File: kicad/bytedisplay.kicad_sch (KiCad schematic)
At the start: 6 parts, among them J1 LObits, J2 HIbits, J3 PGM, U1 ATtiny1616-S, U2 HSN-3621

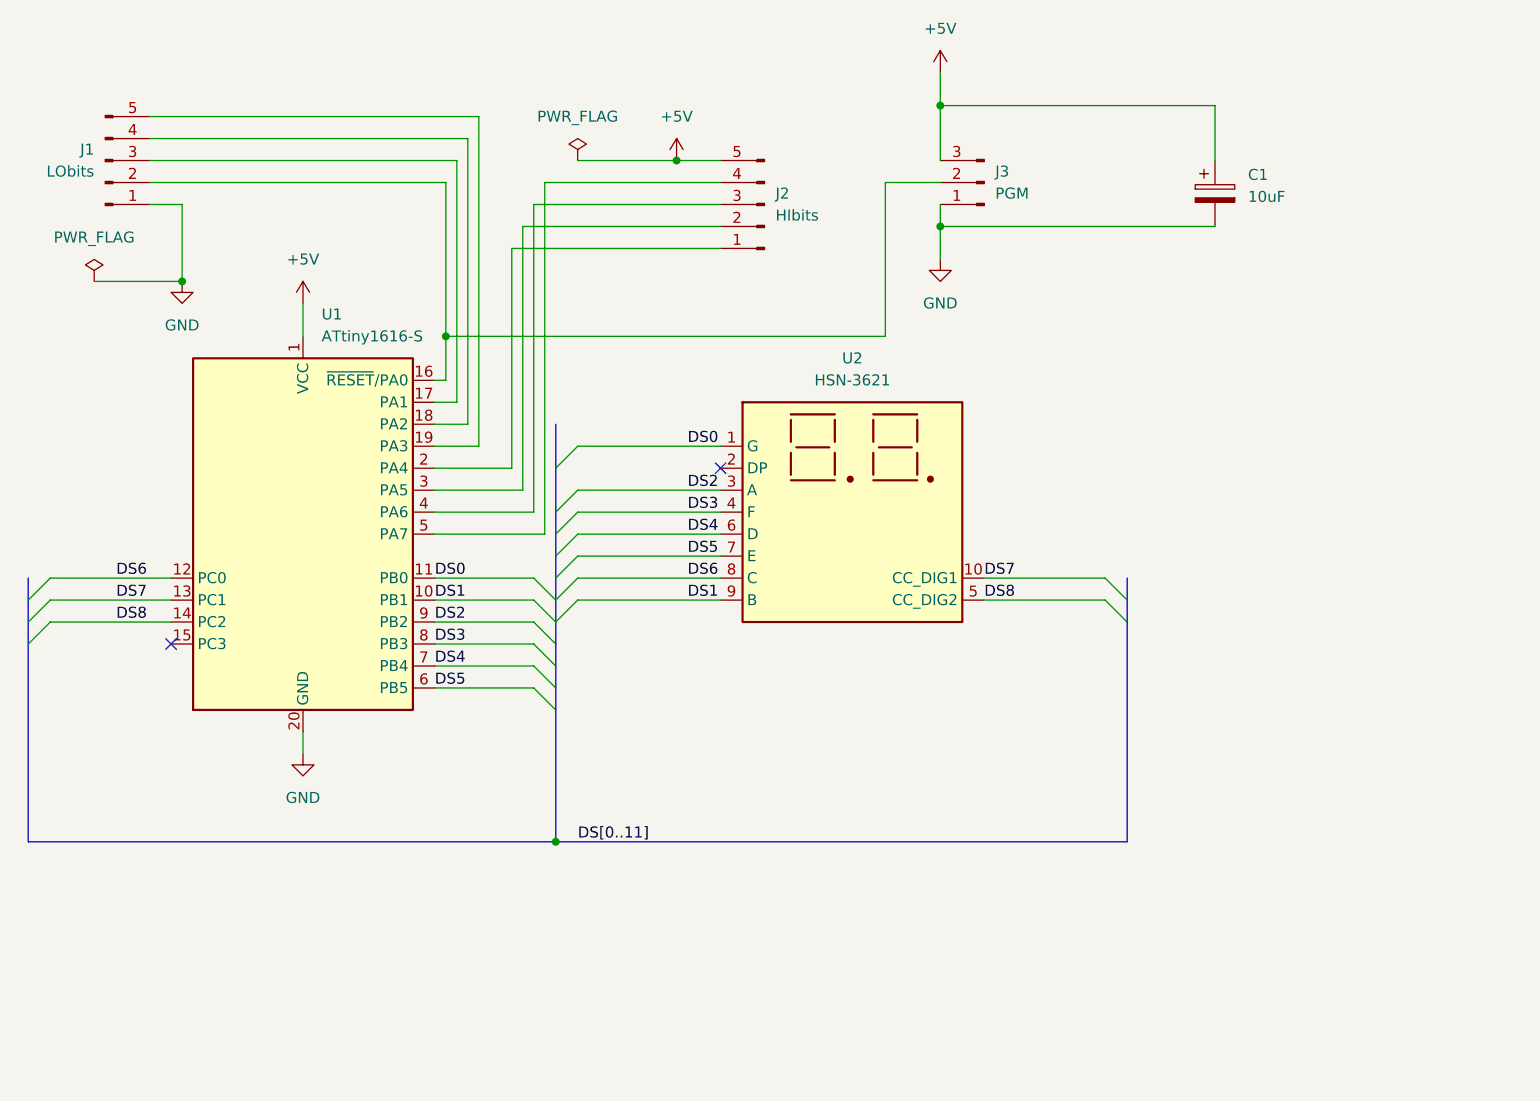
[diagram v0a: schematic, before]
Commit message: [kicad] Move symbols to project library
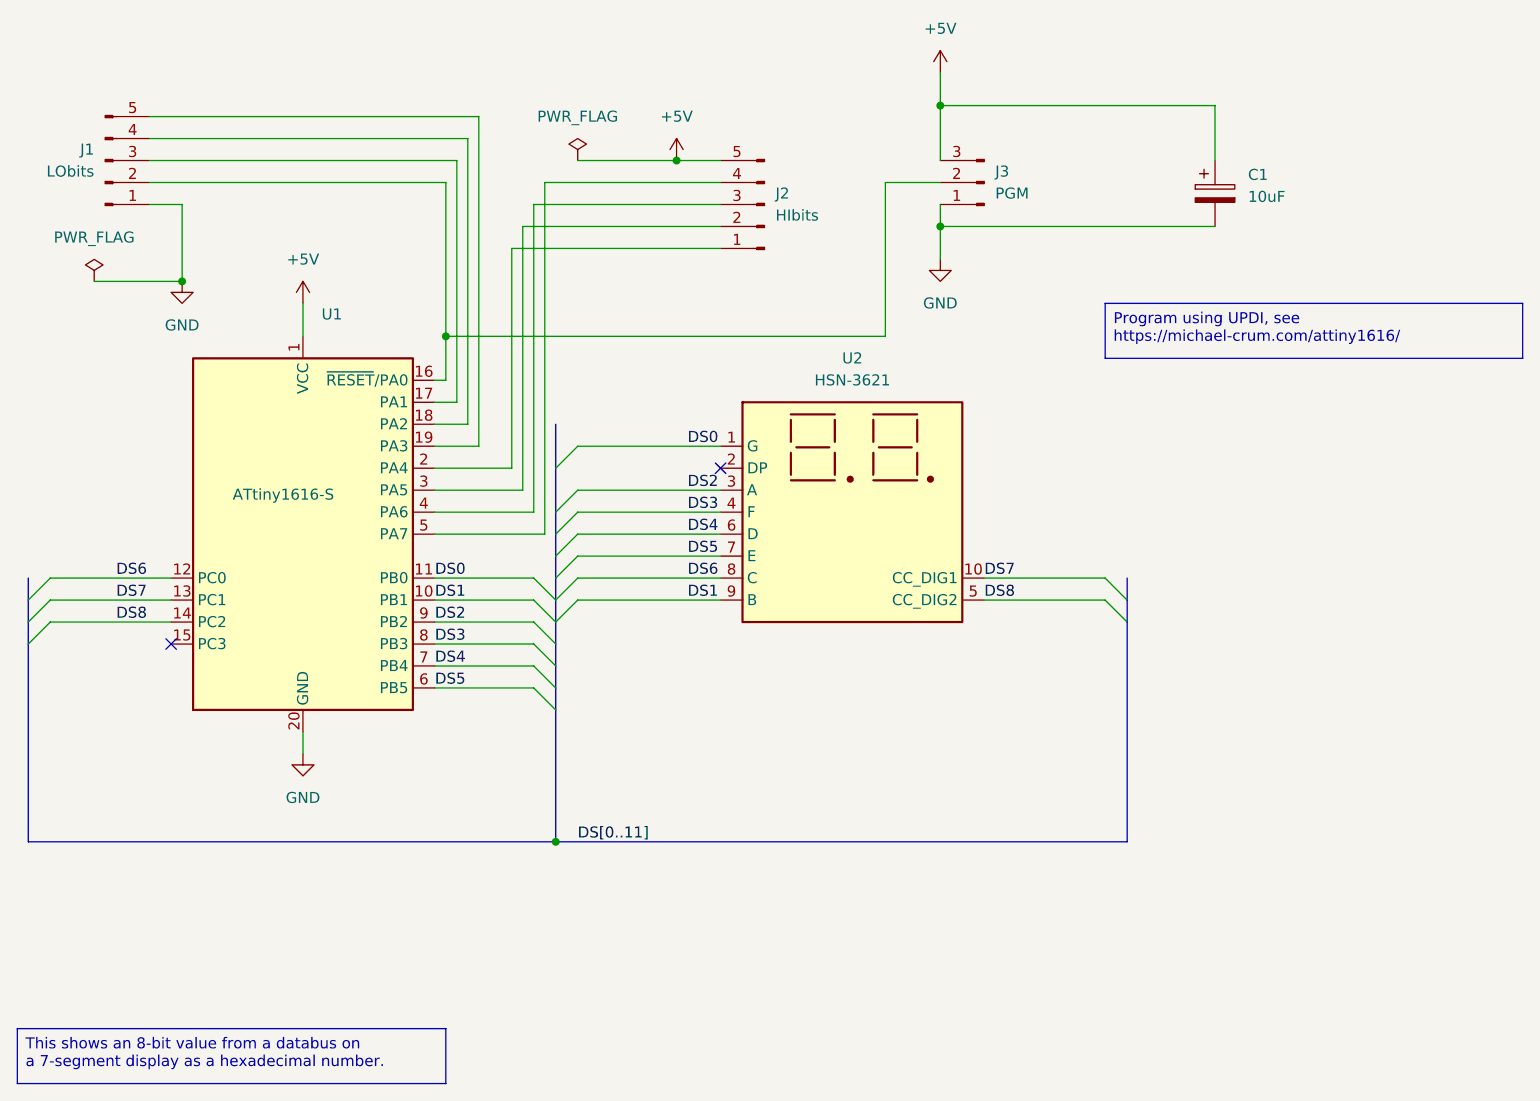
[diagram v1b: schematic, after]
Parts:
- C1: symbol Device:C_Polarized -> Library:C_Polarized
- J1, J2: symbol Connector:Conn_01x05_Pin -> Library:Conn_01x05_Pin
- J3: symbol Connector:Conn_01x03_Pin -> Library:Conn_01x03_Pin
- U1: symbol MCU_Microchip_ATtiny:ATtiny1616-S -> Library:ATtiny1616-S
- U2: symbol Display_Character:HDSM-443B -> Library:HDSM-443B
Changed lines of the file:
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@@
 		(company "ErrorSoft")
+	)
+	(text_box "This shows an 8-bit value from a databus on\na 7-segment display as a hexadecimal number."
+		(exclude_from_sim no)
+		(at 45.72 149.86 0)
+		(size 49.53 6.35)
+		(margins 0.9525 0.9525 0.9525 0.9525)
+		(stroke
+			(width 0)
+			(type solid)
+		)
+		(fill
+			(type none)
+		)
+		(effects
+			(font
+				(size 1.27 1.27)
+			)
+			(justify left top)
+		)
+	)
+	(text_box "Program using UPDI, see\nhttps://michael-crum.com/attiny1616/"
+		(exclude_from_sim no)
+		(at 171.45 66.04 0)
+		(size 48.26 6.35)
+		(margins 0.9525 0.9525 0.9525 0.9525)
+		(stroke
+			(width 0)
+			(type solid)
+		)
+		(fill
+			(type color)
+			(color 0 255 0 1)
+		)
+		(effects
+			(font
+				(size 1.27 1.27)
+			)
+			(justify left top)
+		)
 	)
 	(junction
@@
 	)
 	(symbol
-		(lib_id "Device:C_Polarized")
+		(lib_id "Library:C_Polarized")
 		(at 184.15 53.34 0)
 		(unit 1)
@@
 	)
 	(symbol
-		(lib_id "Display_Character:HDSM-443B")
+		(lib_id "Library:HDSM-443B")
 		(at 142.24 90.17 0)
 		(unit 1)
@@
 	)
 	(symbol
-		(lib_id "MCU_Microchip_ATtiny:ATtiny1616-S")
+		(lib_id "Library:ATtiny1616-S")
 		(at 78.74 92.71 0)
 		(unit 1)
@@
 		(on_board yes)
 		(dnp no)
-		(fields_autoplaced yes)
 		(property "Reference" "U1"
 			(at 80.8833 67.31 0)
@@
 		)
 		(property "Value" "ATtiny1616-S"
-			(at 80.8833 69.85 0)
+			(at 70.612 88.138 0)
 			(effects
 				(font
@@
 	)
 	(symbol
-		(lib_id "Connector:Conn_01x03_Pin")
+		(lib_id "Library:Conn_01x03_Pin")
 		(at 157.48 52.07 180)
 		(unit 1)
@@
 	)
 	(symbol
-		(lib_id "Connector:Conn_01x05_Pin")
+		(lib_id "Library:Conn_01x05_Pin")
 		(at 55.88 49.53 0)
 		(mirror x)
@@
 	)
 	(symbol
-		(lib_id "Connector:Conn_01x05_Pin")
+		(lib_id "Library:Conn_01x05_Pin")
 		(at 132.08 54.61 180)
 		(unit 1)
